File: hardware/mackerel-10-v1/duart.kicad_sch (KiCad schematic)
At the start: 9 parts, among them J12 Conn_02x10_Odd_Even, J4 Conn_01x06, J5 Conn_01x06, U14 XR68C681, X3 3.6864MHz

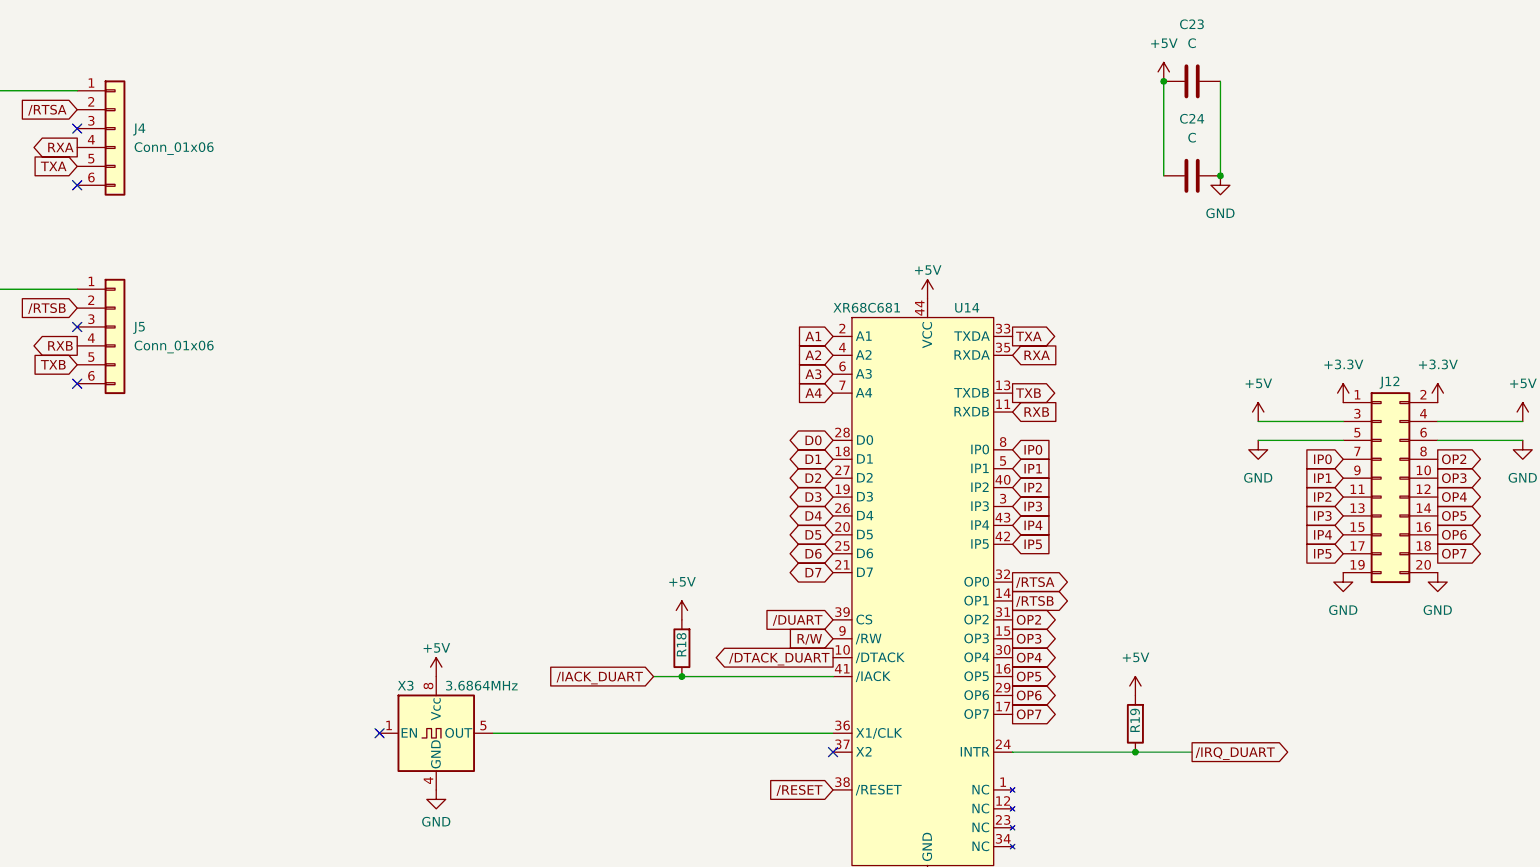
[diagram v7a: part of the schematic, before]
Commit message: Remove BERR from CPLD
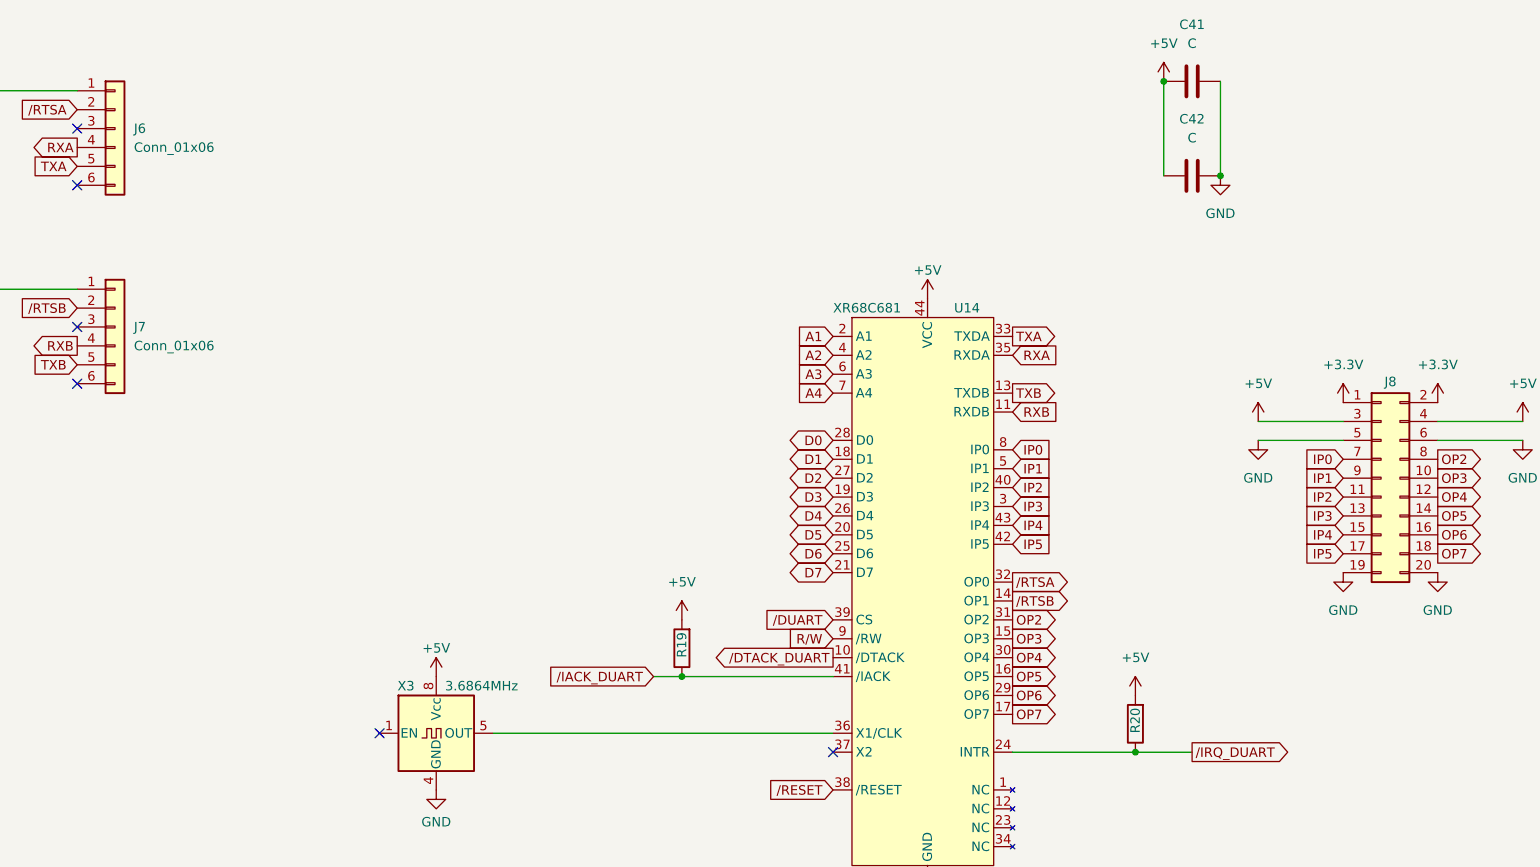
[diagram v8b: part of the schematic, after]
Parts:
- renumbered C23 to C41, C24 to C42, J4 to J6, J5 to J7, J12 to J8, R18 to R19, R19 to R20
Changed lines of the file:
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@@
 		(dnp no)
 		(fields_autoplaced yes)
-		(property "Reference" "#PWR048"
+		(property "Reference" "#PWR069"
 			(at 44.45 36.83 0)
 			(effects
@@
 			(project ""
 				(path "/0a8f74be-008b-4256-a2d9-73a458311ea0/a13f62d4-3d46-4322-adb3-03a373f47e08"
-					(reference "#PWR048")
+					(reference "#PWR069")
 					(unit 1)
 				)
@@
 		(dnp no)
 		(fields_autoplaced yes)
-		(property "Reference" "#PWR0110"
+		(property "Reference" "#PWR085"
 			(at 257.81 78.74 0)
 			(effects
@@
 			(project "mackerel-10-v1"
 				(path "/0a8f74be-008b-4256-a2d9-73a458311ea0/a13f62d4-3d46-4322-adb3-03a373f47e08"
-					(reference "#PWR0110")
+					(reference "#PWR085")
 					(unit 1)
 				)
@@
 		(on_board yes)
 		(dnp no)
-		(property "Reference" "R19"
+		(property "Reference" "R20"
 			(at 205.74 116.84 90)
 			(effects
@@
 			(project "mackerel-10-v1"
 				(path "/0a8f74be-008b-4256-a2d9-73a458311ea0/a13f62d4-3d46-4322-adb3-03a373f47e08"
-					(reference "R19")
+					(reference "R20")
 					(unit 1)
 				)
@@
 		(dnp no)
 		(fields_autoplaced yes)
-		(property "Reference" "C23"
+		(property "Reference" "C41"
 			(at 213.36 21.59 90)
 			(effects
@@
 			(project "mackerel-10-v1"
 				(path "/0a8f74be-008b-4256-a2d9-73a458311ea0/a13f62d4-3d46-4322-adb3-03a373f47e08"
-					(reference "C23")
+					(reference "C41")
 					(unit 1)
 				)
@@
 		(dnp no)
 		(fields_autoplaced yes)
-		(property "Reference" "#PWR0111"
+		(property "Reference" "#PWR086"
 			(at 257.81 83.82 0)
 			(effects
@@
 			(project "mackerel-10-v1"
 				(path "/0a8f74be-008b-4256-a2d9-73a458311ea0/a13f62d4-3d46-4322-adb3-03a373f47e08"
-					(reference "#PWR0111")
+					(reference "#PWR086")
 					(unit 1)
 				)
@@
 		(on_board yes)
 		(dnp no)
-		(property "Reference" "#PWR053"
+		(property "Reference" "#PWR072"
 			(at 111.76 130.81 0)
 			(effects
@@
 			(project "mackerel-10-v1"
 				(path "/0a8f74be-008b-4256-a2d9-73a458311ea0/a13f62d4-3d46-4322-adb3-03a373f47e08"
-					(reference "#PWR053")
+					(reference "#PWR072")
 					(unit 1)
 				)
@@
 		(dnp no)
 		(fields_autoplaced yes)
-		(property "Reference" "#PWR0115"
+		(property "Reference" "#PWR084"
 			(at 246.38 101.6 0)
 			(effects
@@
 			(project "mackerel-10-v1"
 				(path "/0a8f74be-008b-4256-a2d9-73a458311ea0/a13f62d4-3d46-4322-adb3-03a373f47e08"
-					(reference "#PWR0115")
+					(reference "#PWR084")
 					(unit 1)
 				)
@@
 		(on_board yes)
 		(dnp no)
-		(property "Reference" "#PWR052"
+		(property "Reference" "#PWR071"
 			(at 111.76 113.03 0)
 			(effects
@@
 			(project "mackerel-10-v1"
 				(path "/0a8f74be-008b-4256-a2d9-73a458311ea0/a13f62d4-3d46-4322-adb3-03a373f47e08"
-					(reference "#PWR052")
+					(reference "#PWR071")
 					(unit 1)
 				)
@@
 		(dnp no)
 		(fields_autoplaced yes)
-		(property "Reference" "#PWR054"
+		(property "Reference" "#PWR073"
 			(at 144.78 105.41 0)
 			(effects
@@
 			(project "mackerel-10-v1"
 				(path "/0a8f74be-008b-4256-a2d9-73a458311ea0/a13f62d4-3d46-4322-adb3-03a373f47e08"
-					(reference "#PWR054")
+					(reference "#PWR073")
 					(unit 1)
 				)
@@
 		(dnp no)
 		(fields_autoplaced yes)
-		(property "Reference" "#PWR049"
+		(property "Reference" "#PWR070"
 			(at 44.45 63.5 0)
 			(effects
@@
 			(project "mackerel-10-v1"
 				(path "/0a8f74be-008b-4256-a2d9-73a458311ea0/a13f62d4-3d46-4322-adb3-03a373f47e08"
-					(reference "#PWR049")
+					(reference "#PWR070")
 					(unit 1)
 				)
@@
 		(dnp no)
 		(fields_autoplaced yes)
-		(property "Reference" "#PWR0113"
+		(property "Reference" "#PWR083"
 			(at 246.38 76.2 0)
 			(effects
@@
 			(project "mackerel-10-v1"
 				(path "/0a8f74be-008b-4256-a2d9-73a458311ea0/a13f62d4-3d46-4322-adb3-03a373f47e08"
-					(reference "#PWR0113")
+					(reference "#PWR083")
 					(unit 1)
 				)
@@
 		(dnp no)
 		(fields_autoplaced yes)
-		(property "Reference" "#PWR0109"
+		(property "Reference" "#PWR079"
 			(at 222.25 78.74 0)
 			(effects
@@
 			(project ""
 				(path "/0a8f74be-008b-4256-a2d9-73a458311ea0/a13f62d4-3d46-4322-adb3-03a373f47e08"
-					(reference "#PWR0109")
+					(reference "#PWR079")
 					(unit 1)
 				)
@@
 		(on_board yes)
 		(dnp no)
-		(property "Reference" "#PWR055"
+		(property "Reference" "#PWR074"
 			(at 177.8 62.23 0)
 			(effects
@@
 			(project "mackerel-10-v1"
 				(path "/0a8f74be-008b-4256-a2d9-73a458311ea0/a13f62d4-3d46-4322-adb3-03a373f47e08"
-					(reference "#PWR055")
+					(reference "#PWR074")
 					(unit 1)
 				)
@@
 		(dnp no)
 		(fields_autoplaced yes)
-		(property "Reference" "J4"
+		(property "Reference" "J6"
 			(at 71.12 35.5599 0)
 			(effects
@@
 			(project ""
 				(path "/0a8f74be-008b-4256-a2d9-73a458311ea0/a13f62d4-3d46-4322-adb3-03a373f47e08"
-					(reference "J4")
+					(reference "J6")
 					(unit 1)
 				)
@@
 		(on_board yes)
 		(dnp no)
-		(property "Reference" "J12"
+		(property "Reference" "J8"
 			(at 240.03 69.596 0)
 			(effects
@@
 			(project ""
 				(path "/0a8f74be-008b-4256-a2d9-73a458311ea0/a13f62d4-3d46-4322-adb3-03a373f47e08"
-					(reference "J12")
+					(reference "J8")
 					(unit 1)
 				)
@@
 		(dnp no)
 		(fields_autoplaced yes)
-		(property "Reference" "C24"
+		(property "Reference" "C42"
 			(at 213.36 34.29 90)
 			(effects
@@
 			(project "mackerel-10-v1"
 				(path "/0a8f74be-008b-4256-a2d9-73a458311ea0/a13f62d4-3d46-4322-adb3-03a373f47e08"
-					(reference "C24")
+					(reference "C42")
 					(unit 1)
 				)
@@
 		(dnp no)
 		(fields_autoplaced yes)
-		(property "Reference" "#PWR084"
+		(property "Reference" "#PWR077"
 			(at 209.55 33.02 0)
 			(effects
@@
 			(project "mackerel-10-v1"
 				(path "/0a8f74be-008b-4256-a2d9-73a458311ea0/a13f62d4-3d46-4322-adb3-03a373f47e08"
-					(reference "#PWR084")
+					(reference "#PWR077")
 					(unit 1)
 				)
@@
 		(dnp no)
 		(fields_autoplaced yes)
-		(property "Reference" "#PWR0114"
+		(property "Reference" "#PWR082"
 			(at 233.68 101.6 0)
 			(effects
@@
 			(project ""
 				(path "/0a8f74be-008b-4256-a2d9-73a458311ea0/a13f62d4-3d46-4322-adb3-03a373f47e08"
-					(reference "#PWR0114")
+					(reference "#PWR082")
 					(unit 1)
 				)
@@
 		(dnp no)
 		(fields_autoplaced yes)
-		(property "Reference" "#PWR0112"
+		(property "Reference" "#PWR081"
 			(at 233.68 76.2 0)
 			(effects
@@
 			(project ""
 				(path "/0a8f74be-008b-4256-a2d9-73a458311ea0/a13f62d4-3d46-4322-adb3-03a373f47e08"
-					(reference "#PWR0112")
+					(reference "#PWR081")
 					(unit 1)
 				)
@@
 		(dnp no)
 		(fields_autoplaced yes)
-		(property "Reference" "#PWR086"
+		(property "Reference" "#PWR078"
 			(at 217.17 48.26 0)
 			(effects
@@
 			(project "mackerel-10-v1"
 				(path "/0a8f74be-008b-4256-a2d9-73a458311ea0/a13f62d4-3d46-4322-adb3-03a373f47e08"
-					(reference "#PWR086")
+					(reference "#PWR078")
 					(unit 1)
 				)
@@
 		(dnp no)
 		(fields_autoplaced yes)
-		(property "Reference" "#PWR057"
+		(property "Reference" "#PWR080"
 			(at 222.25 83.82 0)
 			(effects
@@
 			(project ""
 				(path "/0a8f74be-008b-4256-a2d9-73a458311ea0/a13f62d4-3d46-4322-adb3-03a373f47e08"
-					(reference "#PWR057")
+					(reference "#PWR080")
 					(unit 1)
 				)
@@
 		(dnp no)
 		(fields_autoplaced yes)
-		(property "Reference" "J5"
+		(property "Reference" "J7"
 			(at 71.12 62.2299 0)
 			(effects
@@
 			(project "mackerel-10-v1"
 				(path "/0a8f74be-008b-4256-a2d9-73a458311ea0/a13f62d4-3d46-4322-adb3-03a373f47e08"
-					(reference "J5")
+					(reference "J7")
 					(unit 1)
 				)
@@
 		(on_board yes)
 		(dnp no)
-		(property "Reference" "R18"
+		(property "Reference" "R19"
 			(at 144.78 106.68 90)
 			(effects
@@
 			(project "mackerel-10-v1"
 				(path "/0a8f74be-008b-4256-a2d9-73a458311ea0/a13f62d4-3d46-4322-adb3-03a373f47e08"
-					(reference "R18")
+					(reference "R19")
 					(unit 1)
 				)
@@
 		(dnp no)
 		(fields_autoplaced yes)
-		(property "Reference" "#PWR058"
+		(property "Reference" "#PWR076"
 			(at 205.74 115.57 0)
 			(effects
@@
 			(project ""
 				(path "/0a8f74be-008b-4256-a2d9-73a458311ea0/a13f62d4-3d46-4322-adb3-03a373f47e08"
-					(reference "#PWR058")
+					(reference "#PWR076")
 					(unit 1)
 				)
@@
 		(dnp no)
 		(fields_autoplaced yes)
-		(property "Reference" "#PWR056"
+		(property "Reference" "#PWR075"
 			(at 177.8 143.51 0)
 			(effects
@@
 			(project "mackerel-10-v1"
 				(path "/0a8f74be-008b-4256-a2d9-73a458311ea0/a13f62d4-3d46-4322-adb3-03a373f47e08"
-					(reference "#PWR056")
-					(unit 1)
-				)
+					(reference "#PWR075")
+					(unit 1)
+				)
